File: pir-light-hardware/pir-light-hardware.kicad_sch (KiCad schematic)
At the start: 44 parts, among them J1 ZH1.5-3, J2 ZH1.5-3, Q1 AON7240, Q2 NPN, Q3 PNP, Q4 PNP, U1 M74VHC1GT08DFT2G, U2 LMV331IDCKR, U3 AS312

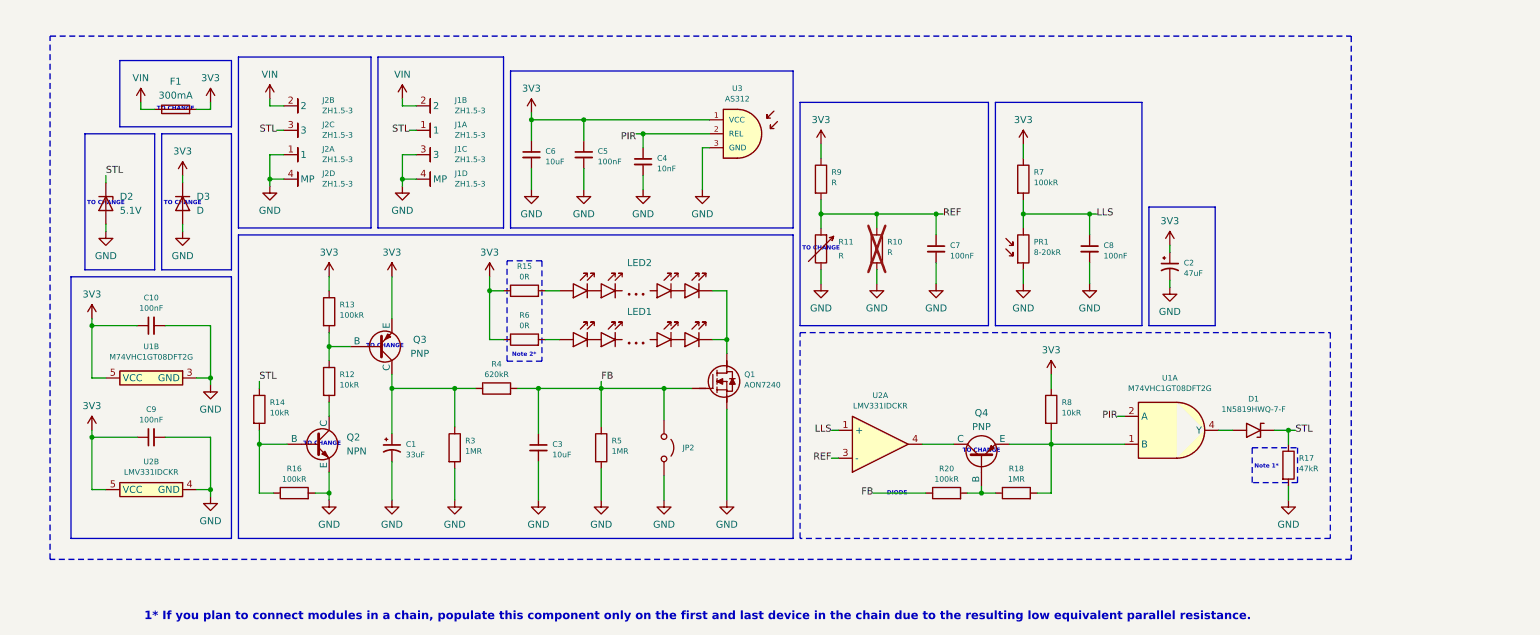
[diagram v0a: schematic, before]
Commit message: chore: rework sustain feature, add actual components to schematic
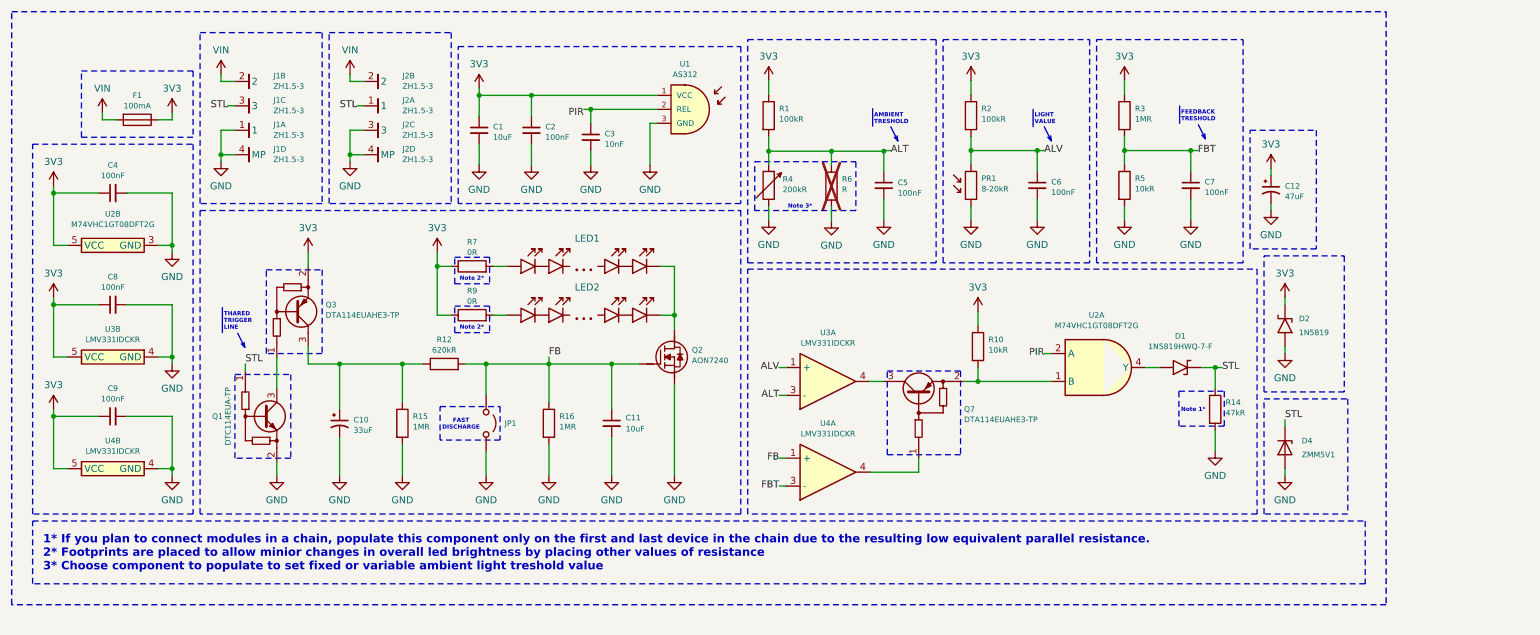
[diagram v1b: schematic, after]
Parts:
- removed C3: 10uF, REST:C_0603_1608Metric, symbol REST:C_MLCC
- removed D2: 5.1V, symbol Device:D_Zener
- removed D3: D, symbol Device:D
- removed F1: 300mA, symbol Device:Fuse
- removed JP2: Jumper_Open, REST:SolderJumper-2_P1.3mm_Open_RoundedPad1.0x1.5mm, symbol REST:Jumper_Open
- removed Q2: NPN, symbol Simulation_SPICE:NPN
- removed Q3, Q4: PNP, symbol Simulation_SPICE:PNP
- removed R12, R14: 10kR, REST:R_0402_1005Metric, symbol REST:R
- removed R13, R16, R20: 100kR, REST:R_0402_1005Metric, symbol REST:R
- removed R18: 1MR, REST:R_0402_1005Metric, symbol REST:R
- added C11: 10uF, REST:C_0603_1608Metric, symbol REST:C_MLCC
- added C7, C9: 100nF, REST:C_0402_1005Metric, symbol REST:C_MLCC
- added D2: 1N5819, Diode_SMD:D_SOD-123F, symbol 1N5819HWQ-7-F:1N5819HWQ-7-F
- added D4: ZMM5V1, Diode_SMD:D_MiniMELF, symbol Diode:ZMMxx
- added F1: 100mA, symbol REST:Fuse
- added JP1: Jumper_Open, REST:SolderJumper-2_P1.3mm_Open_RoundedPad1.0x1.5mm, symbol REST:Jumper_Open
- added Q1: DTC114EUA-TP, SOT65P228X120-3N, symbol DTC114EUA-TP:DTC114EUA-TP
- added Q3: DTA114EUAHE3-TP, DTA114EUAHE3-TP:SOT65P228X120-3N, symbol DTA114EUAHE3-TP:DTA114EUAHE3-TPv2
- added Q7: DTA114EUAHE3-TP, DTA114EUAHE3-TP:SOT65P228X120-3N, symbol DTA114EUAHE3-TP:DTA114EUAHE3-TP
- added R3: 1MR, REST:R_0402_1005Metric, symbol REST:R
- added R5: 10kR, REST:R_0402_1005Metric, symbol REST:R
- added U4: LMV331IDCKR, M74VHC1GT08D:SOT65P210X110-5N, symbol LMV331IDCKR:LMV331IDCKR
- R1: renamed from R9; value R -> 100kR
- R4: renamed from R11; value R -> 200kR; footprint (none) -> REST:Potentiometer_Bourns_TC33X_Vertical
- renumbered C6 to C1, C1 to C10, C2 to C12, C5 to C2, C4 to C3, C10 to C4, C7 to C5, C8 to C6, C9 to C8, J2 to J1, J1 to J2, LED2 to LED1, LED1 to LED2, Q1 to Q2, R8 to R10, R4 to R12, R17 to R14, R3 to R15, R5 to R16, R7 to R2, R10 to R6, R15 to R7, R6 to R9, U3 to U1, U1 to U2, U2 to U3
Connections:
- net 3V3: now also C9.1, D2.1 (K), F1.2, Q3.2 (GND), R3.1, U4.5 (VCC)
- net FB: now also C11.1, JP1.1 (A), U4.1 (+)
- net GND: now also C11.2, C7.2, C9.2, D2.2 (A), D4.2 (A), JP1.2 (B), Q1.2 (GND), R5.2, U4.4 (GND)
- net STL: now also D4.1 (K), Q1.1 (IN)
- net VIN: now also F1.1
- net at R10.2, U2.1 (B): now also Q7.2 (GND)
- net at U3.4: now also Q7.3 (OUT)
- net at C10.1, R12.1, R15.1: now also Q3.3 (OUT)
- net LLS renamed ALV
- net REF renamed ALT
- new net: Q7.1 (IN), U4.4
- new net: Q1.3 (OUT), Q3.1 (IN)
- new net FBT: C7.1, R3.2, R5.1, U4.3 (-)
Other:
- note added: "1* If you plan to connect modules in a chain, populate this component only on the first and last device in the chain due to the resulting low equivalent parallel resistance. 2* Footprints are placed to allow minior changes in overall led brightness by placing other values of resistance 3* Choose component to populate to set fixed or variable ambient light treshold value"
- note added: "AMBIENT TRESHOLD"
- note added: "FAST DISCHARGE"
- note added: "FEEDBACK TRESHOLD"
- note added: "LIGHT VALUE"
- note added: "Note 3*"
- note added: "THARED TRIGGER LINE"
- note removed: "1* If you plan to connect modules in a chain, populate this component only on the first and last device in the chain due to the resulting low equivalent parallel resistance."
- note removed: "DIODE"
- note removed: "TO CHANGE"
- moved on the sheet: C1, C10, C12, C2, C3, C4, C5, C6, C8, D1, J1A, J1B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
